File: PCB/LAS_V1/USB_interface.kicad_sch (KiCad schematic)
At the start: 3 parts, among them P1 USB_C_Plug

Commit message: installing JLB, PCB mostly done
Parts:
- removed D4: D_Schottky, symbol Device:D_Schottky
- removed P1: USB_C_Plug, symbol Connector:USB_C_Plug
- removed R5: 5.1k, symbol Device:R_Small_US
- added C10: 100uF, symbol Device:C_Small
- added C11, C7: 1uF/16V (10%), symbol Device:C_Small
- added C8, C9: 1uF, symbol Device:C_Small
- added D7: 1N5819WS, symbol Device:D_Schottky
- added J7: USB_C_Receptacle_USB2.0, symbol Connector:USB_C_Receptacle_USB2.0
- added Q2, Q3: MMBT2222A, symbol Simulation_SPICE:NPN
- added R10: 10k (1%), symbol Device:R_Small_US
- added R11, R12: 10k, symbol Device:R_Small_US
- added R8, R9: 5.1k, symbol Device:R_Small_US
- added U3: CH343P, Package_DFN_QFN:TQFN-16-1EP_3x3mm_P0.5mm_EP1.6x1.6mm, symbol Custom:CH343P
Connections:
- net GND: now also C10.2, C11.2, C7.2, C8.2, C9.2, J7.A1 (GND), J7.A12 (GND), J7.B1 (GND), J7.B12 (GND), R8.2, R9.2, U3.0 (GND), U3.17 (EP), U3.2 (GND)
- net VBus: now also C7.1, C9.1, D7.2 (A), J7.A4 (VBUS), J7.A9 (VBUS), J7.B4 (VBUS), J7.B9 (VBUS), U3.3 (VDD5), U3.4 (V3), U3.9 (VBUS)
- new net: Q2.2 (B), R12.2
- new net: C10.1, U3.6 (V3)
- new net: J7.A6 (D+), J7.B6 (D+), U3.7 (UD+)
- new net: J7.A7 (D-), J7.B7 (D-), U3.8 (UD-)
- new net: Q3.2 (B), R11.2
- new net: J7.B5 (CC2), R9.1
- new net: J7.A5 (CC1), R8.1
- new net +3.3V: C8.1, R10.1, U3.1 (VIO)
- new net BOOT_SEL: Q3.1 (C)
- new net CHIP_PU: C11.1, Q2.1 (C), R10.2
- new net DTR: Q3.3 (E), R12.1, U3.12 (DTR)
- new net RTS: Q2.3 (E), R11.1, U3.13 (RTS)
- new net RXD0: U3.4 (V3)
- new net TXD0: U3.5 (RXD)
- new net VCC_5V: D7.1 (K)
- no-connect marks 2 -> 8
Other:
- note added: "RTC_GPIO18, GPIO18, U1RXD, ADC2_CH7, DAC_2, CLK_OUT3"

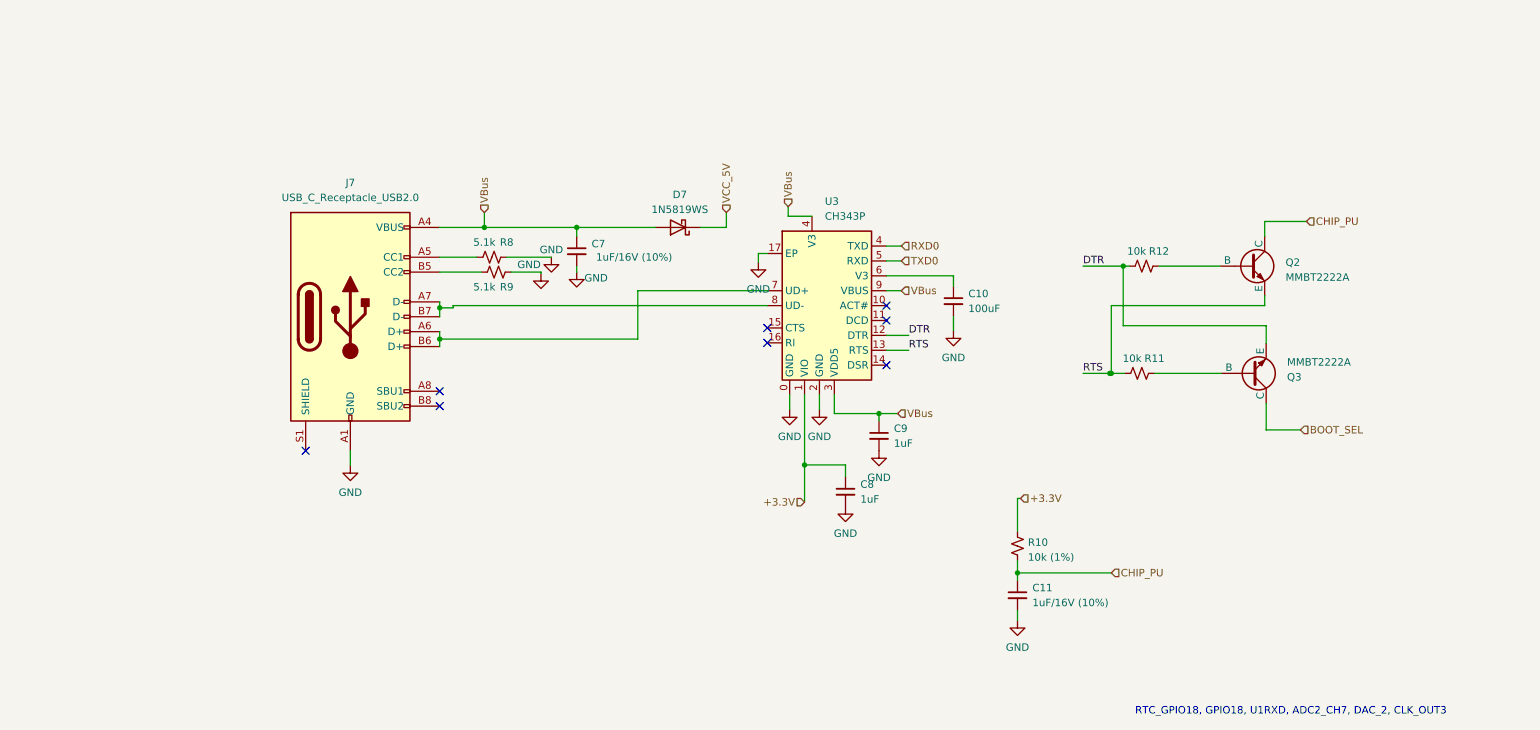
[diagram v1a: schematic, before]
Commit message: added JLBPCB part Numbers
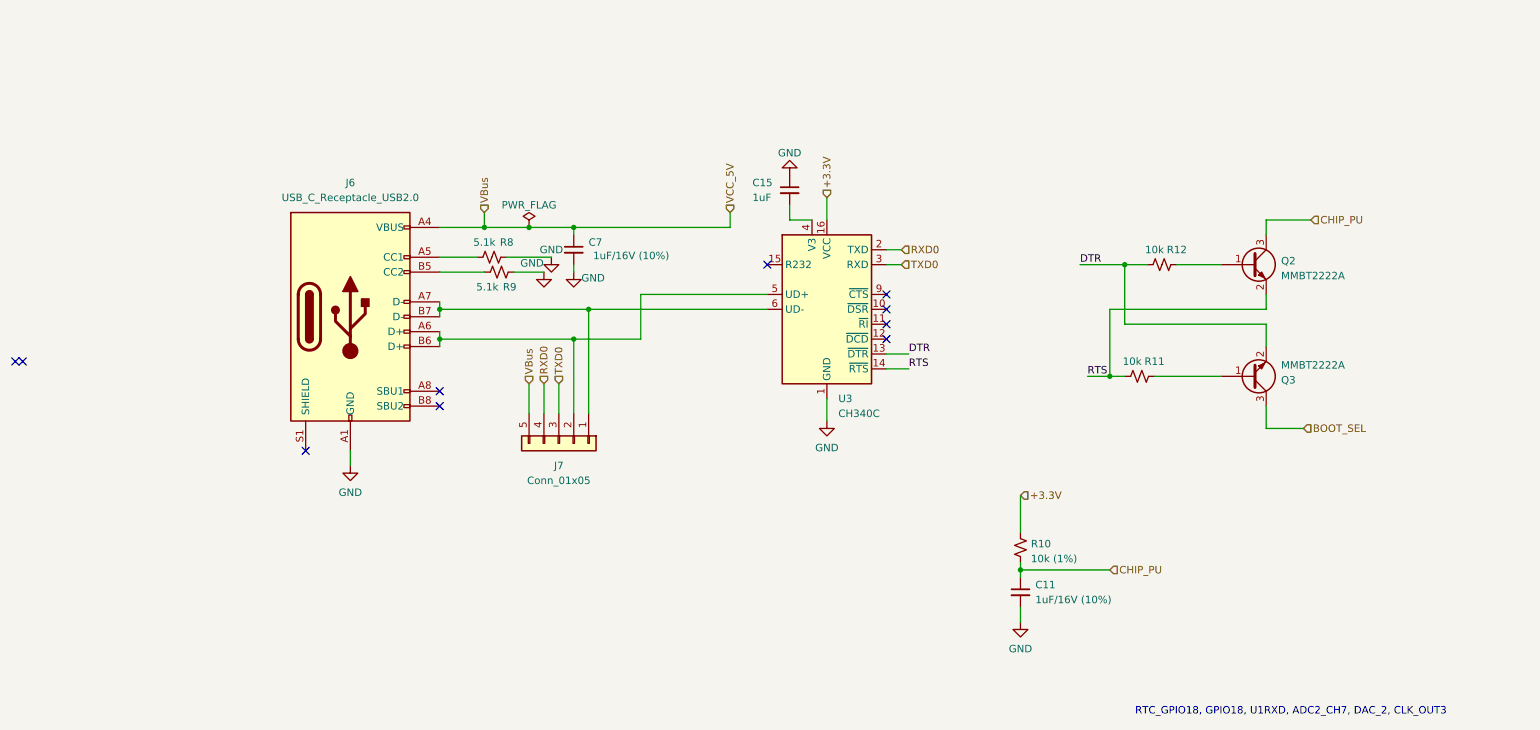
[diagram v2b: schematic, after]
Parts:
- removed C10: 100uF, symbol Device:C_Small
- removed C8, C9: 1uF, symbol Device:C_Small
- removed D7: 1N5819WS, symbol Device:D_Schottky
- removed Q2, Q3: MMBT2222A, symbol Simulation_SPICE:NPN
- removed U3: CH343P, Package_DFN_QFN:TQFN-16-1EP_3x3mm_P0.5mm_EP1.6x1.6mm, symbol Custom:CH343P
- added C15: 1uF, Capacitor_SMD:C_0603_1608Metric, symbol Device:C_Small
- added J7: Conn_01x05, Connector_PinHeader_1.27mm:PinHeader_1x05_P1.27mm_Vertical, symbol Connector_Generic:Conn_01x05
- added Q2, Q3: MMBT2222A, Package_TO_SOT_SMD:SOT-23, symbol Transistor_BJT:MMBT3904
- added U3: CH340C, Package_SO:SOIC-16_3.9x9.9mm_P1.27mm, symbol Interface_USB:CH340C
- C11, C7: footprint (none) -> Capacitor_SMD:C_0603_1608Metric; LCSC (none) -> C15849
- J6: renamed from J7; footprint (none) -> Custom:USB-C_SMD-TYPE-C-31-M-12; LCSC (none) -> C2927038
- R10: footprint (none) -> Resistor_SMD:R_0603_1608Metric; LCSC (none) -> C25804
- R11, R12: footprint (none) -> Resistor_SMD:R_1206_3216Metric; LCSC (none) -> C17902
- R8, R9: footprint (none) -> Resistor_SMD:R_0603_1608Metric; LCSC (none) -> C23186
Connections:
- net +3.3V: now also U3.16 (VCC)
- net BOOT_SEL: now also Q3.3 (C)
- net CHIP_PU: now also Q2.3 (C)
- net DTR: now also Q3.2 (E), U3.13 (~{DTR})
- net GND: now also C15.1, U3.1 (GND)
- net RTS: now also Q2.2 (E), U3.14 (~{RTS})
- net RXD0: now also J7.4 (Pin_4), U3.2 (TXD)
- net TXD0: now also J7.3 (Pin_3), U3.3 (RXD)
- net VBus: now also J7.5 (Pin_5)
- net at R12.2: now also Q2.1 (B)
- net at J6.A6 (D+), J6.B6 (D+): now also J7.2 (Pin_2), U3.5 (UD+)
- net at J6.A7 (D-), J6.B7 (D-): now also J7.1 (Pin_1), U3.6 (UD-)
- net at R11.2: now also Q3.1 (B)
- new net: C15.2, U3.4 (V3)
- no-connect marks 8 -> 10
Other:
- moved on the sheet: C11, C7, R10, R11, R12, R9

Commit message: All components Placed on PCB
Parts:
- renumbered C15 to C8, C11 to C9, J6 to J7, J7 to J8, R8 to R10, R9 to R11, R10 to R12, R11 to R13, R12 to R14
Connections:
- no-connect marks 10 -> 8
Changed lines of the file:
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@@
   (no_connect (at 101.6 83.82))
   (no_connect (at 157.48 59.69))
-  (no_connect (at 30.48 76.2))
   (no_connect (at 177.8 67.31))
   (no_connect (at 177.8 69.85))
   (no_connect (at 177.8 64.77))
-  (no_connect (at 29.21 76.2))
   (no_connect (at 177.8 72.39))
   (no_connect (at 78.74 91.44))
@@
     (stroke (width 0) (type default))
   )
-  (wire (pts (xy 177.8 77.47) (xy 181.61 77.47))
-    (stroke (width 0) (type default))
-  )
-  (wire (pts (xy 177.8 74.93) (xy 181.61 74.93))
+  (wire (pts (xy 177.8 77.47) (xy 187.96 77.47))
+    (stroke (width 0) (type default))
+  )
+  (wire (pts (xy 177.8 74.93) (xy 187.96 74.93))
     (stroke (width 0) (type default))
   )
@@
     (effects (font (size 1.27 1.27)) (justify left bottom))
   )
-  (label "RTS" (at 181.61 77.47 0) (fields_autoplaced)
+  (label "RTS" (at 187.96 77.47 0) (fields_autoplaced)
     (effects (font (size 1.27 1.27)) (justify left bottom))
   )
-  (label "DTR" (at 181.61 74.93 0) (fields_autoplaced)
+  (label "DTR" (at 187.96 74.93 0) (fields_autoplaced)
     (effects (font (size 1.27 1.27)) (justify left bottom))
   )
@@
   (symbol (lib_id "Device:R_Small_US") (at 224.79 59.69 90) (unit 1)
     (in_bom yes) (on_board yes) (dnp no)
-    (property "Reference" "R12" (at 227.33 57.15 90)
+    (property "Reference" "R14" (at 227.33 57.15 90)
       (effects (font (size 1.27 1.27)))
     )
@@
       (project "LAS_V1"
         (path "/aadef4b8-3115-4a49-998f-828f2021a6b4/a475df9f-c6e9-4f77-bf99-c031d1147f10"
-          (reference "R12") (unit 1)
+          (reference "R14") (unit 1)
         )
       )
@@
   (symbol (lib_id "Connector_Generic:Conn_01x05") (at 121.92 90.17 270) (unit 1)
     (in_bom yes) (on_board yes) (dnp no) (fields_autoplaced)
-    (property "Reference" "J7" (at 121.92 93.98 90)
+    (property "Reference" "J8" (at 121.92 93.98 90)
       (effects (font (size 1.27 1.27)))
     )
@@
       (project "LAS_V1"
         (path "/aadef4b8-3115-4a49-998f-828f2021a6b4/a475df9f-c6e9-4f77-bf99-c031d1147f10"
-          (reference "J7") (unit 1)
+          (reference "J8") (unit 1)
         )
       )
@@
   (symbol (lib_id "Device:C_Small") (at 200.66 115.57 0) (unit 1)
     (in_bom yes) (on_board yes) (dnp no) (fields_autoplaced)
-    (property "Reference" "C11" (at 203.2 114.3063 0)
+    (property "Reference" "C9" (at 203.2 114.3063 0)
       (effects (font (size 1.27 1.27)) (justify left))
     )
@@
       (project "LAS_V1"
         (path "/aadef4b8-3115-4a49-998f-828f2021a6b4/a475df9f-c6e9-4f77-bf99-c031d1147f10"
-          (reference "C11") (unit 1)
+          (reference "C9") (unit 1)
         )
       )
@@
   (symbol (lib_id "power:GND") (at 124.46 60.96 0) (unit 1)
     (in_bom yes) (on_board yes) (dnp no)
-    (property "Reference" "#PWR021" (at 124.46 67.31 0)
+    (property "Reference" "#PWR022" (at 124.46 67.31 0)
       (effects (font (size 1.27 1.27)) hide)
     )
@@
       (project "LAS_V1"
         (path "/aadef4b8-3115-4a49-998f-828f2021a6b4/a475df9f-c6e9-4f77-bf99-c031d1147f10"
-          (reference "#PWR021") (unit 1)
+          (reference "#PWR022") (unit 1)
         )
       )
@@
   (symbol (lib_id "power:GND") (at 120.65 58.42 0) (unit 1)
     (in_bom yes) (on_board yes) (dnp no)
-    (property "Reference" "#PWR020" (at 120.65 64.77 0)
+    (property "Reference" "#PWR021" (at 120.65 64.77 0)
       (effects (font (size 1.27 1.27)) hide)
     )
@@
       (project "LAS_V1"
         (path "/aadef4b8-3115-4a49-998f-828f2021a6b4/a475df9f-c6e9-4f77-bf99-c031d1147f10"
-          (reference "#PWR020") (unit 1)
+          (reference "#PWR021") (unit 1)
         )
       )
@@
   (symbol (lib_id "power:GND") (at 167.64 86.36 0) (unit 1)
     (in_bom yes) (on_board yes) (dnp no) (fields_autoplaced)
-    (property "Reference" "#PWR040" (at 167.64 92.71 0)
+    (property "Reference" "#PWR024" (at 167.64 92.71 0)
       (effects (font (size 1.27 1.27)) hide)
     )
@@
       (project "LAS_V1"
         (path "/aadef4b8-3115-4a49-998f-828f2021a6b4/a475df9f-c6e9-4f77-bf99-c031d1147f10"
-          (reference "#PWR040") (unit 1)
+          (reference "#PWR024") (unit 1)
         )
       )
@@
   (symbol (lib_id "Device:R_Small_US") (at 200.66 107.95 0) (unit 1)
     (in_bom yes) (on_board yes) (dnp no) (fields_autoplaced)
-    (property "Reference" "R10" (at 202.438 107.315 0)
+    (property "Reference" "R12" (at 202.438 107.315 0)
       (effects (font (size 1.27 1.27)) (justify left))
     )
@@
       (project "LAS_V1"
         (path "/aadef4b8-3115-4a49-998f-828f2021a6b4/a475df9f-c6e9-4f77-bf99-c031d1147f10"
-          (reference "R10") (unit 1)
+          (reference "R12") (unit 1)
         )
       )
@@
   (symbol (lib_id "Device:C_Small") (at 161.29 46.99 0) (unit 1)
     (in_bom yes) (on_board yes) (dnp no)
-    (property "Reference" "C15" (at 154.94 45.72 0)
+    (property "Reference" "C8" (at 154.94 45.72 0)
       (effects (font (size 1.27 1.27)) (justify left))
     )
@@
       (project "LAS_V1"
         (path "/aadef4b8-3115-4a49-998f-828f2021a6b4/a475df9f-c6e9-4f77-bf99-c031d1147f10"
-          (reference "C15") (unit 1)
+          (reference "C8") (unit 1)
         )
       )
@@
   (symbol (lib_id "Device:R_Small_US") (at 111.76 60.96 90) (unit 1)
     (in_bom yes) (on_board yes) (dnp no)
-    (property "Reference" "R9" (at 113.538 63.5 90)
+    (property "Reference" "R11" (at 113.538 63.5 90)
       (effects (font (size 1.27 1.27)))
     )
@@
       (project "LAS_V1"
         (path "/aadef4b8-3115-4a49-998f-828f2021a6b4/a475df9f-c6e9-4f77-bf99-c031d1147f10"
-          (reference "R9") (unit 1)
+          (reference "R11") (unit 1)
         )
       )
@@
   (symbol (lib_id "power:PWR_FLAG") (at 116.84 53.34 0) (unit 1)
     (in_bom yes) (on_board yes) (dnp no) (fields_autoplaced)
-    (property "Reference" "#FLG03" (at 116.84 51.435 0)
+    (property "Reference" "#FLG02" (at 116.84 51.435 0)
       (effects (font (size 1.27 1.27)) hide)
     )
@@
       (project "LAS_V1"
         (path "/aadef4b8-3115-4a49-998f-828f2021a6b4/a475df9f-c6e9-4f77-bf99-c031d1147f10"
-          (reference "#FLG03") (unit 1)
+          (reference "#FLG02") (unit 1)
         )
       )
@@
   (symbol (lib_id "power:GND") (at 119.38 60.96 0) (unit 1)
     (in_bom yes) (on_board yes) (dnp no)
-    (property "Reference" "#PWR019" (at 119.38 67.31 0)
+    (property "Reference" "#PWR020" (at 119.38 67.31 0)
       (effects (font (size 1.27 1.27)) hide)
     )
@@
       (project "LAS_V1"
         (path "/aadef4b8-3115-4a49-998f-828f2021a6b4/a475df9f-c6e9-4f77-bf99-c031d1147f10"
-          (reference "#PWR019") (unit 1)
+          (reference "#PWR020") (unit 1)
         )
       )
@@
   (symbol (lib_id "Device:R_Small_US") (at 110.49 58.42 90) (unit 1)
     (in_bom yes) (on_board yes) (dnp no)
-    (property "Reference" "R8" (at 113.03 55.88 90)
+    (property "Reference" "R10" (at 113.03 55.88 90)
       (effects (font (size 1.27 1.27)))
     )
@@
       (project "LAS_V1"
         (path "/aadef4b8-3115-4a49-998f-828f2021a6b4/a475df9f-c6e9-4f77-bf99-c031d1147f10"
-          (reference "R8") (unit 1)
+          (reference "R10") (unit 1)
         )
       )
@@
   (symbol (lib_id "power:GND") (at 86.36 93.98 0) (unit 1)
     (in_bom yes) (on_board yes) (dnp no) (fields_autoplaced)
-    (property "Reference" "#PWR018" (at 86.36 100.33 0)
+    (property "Reference" "#PWR019" (at 86.36 100.33 0)
       (effects (font (size 1.27 1.27)) hide)
     )
@@
       (project "LAS_V1"
         (path "/aadef4b8-3115-4a49-998f-828f2021a6b4/a475df9f-c6e9-4f77-bf99-c031d1147f10"
-          (reference "#PWR018") (unit 1)
+          (reference "#PWR019") (unit 1)
         )
       )
@@
   (symbol (lib_id "Connector:USB_C_Receptacle_USB2.0") (at 86.36 68.58 0) (unit 1)
     (in_bom yes) (on_board yes) (dnp no) (fields_autoplaced)
-    (property "Reference" "J6" (at 86.36 45.72 0)
+    (property "Reference" "J7" (at 86.36 45.72 0)
       (effects (font (size 1.27 1.27)))
     )
@@
       (project "LAS_V1"
         (path "/aadef4b8-3115-4a49-998f-828f2021a6b4/a475df9f-c6e9-4f77-bf99-c031d1147f10"
-          (reference "J6") (unit 1)
+          (reference "J7") (unit 1)
         )
       )
@@
   (symbol (lib_id "power:GND") (at 161.29 44.45 180) (unit 1)
     (in_bom yes) (on_board yes) (dnp no) (fields_autoplaced)
-    (property "Reference" "#PWR022" (at 161.29 38.1 0)
+    (property "Reference" "#PWR023" (at 161.29 38.1 0)
       (effects (font (size 1.27 1.27)) hide)
     )
@@
       (project "LAS_V1"
         (path "/aadef4b8-3115-4a49-998f-828f2021a6b4/a475df9f-c6e9-4f77-bf99-c031d1147f10"
-          (reference "#PWR022") (unit 1)
+          (reference "#PWR023") (unit 1)
         )
       )
@@
   (symbol (lib_id "power:GND") (at 200.66 120.65 0) (unit 1)
     (in_bom yes) (on_board yes) (dnp no) (fields_autoplaced)
-    (property "Reference" "#PWR028" (at 200.66 127 0)
+    (property "Reference" "#PWR025" (at 200.66 127 0)
       (effects (font (size 1.27 1.27)) hide)
     )
@@
       (project "LAS_V1"
         (path "/aadef4b8-3115-4a49-998f-828f2021a6b4/a475df9f-c6e9-4f77-bf99-c031d1147f10"
-          (reference "#PWR028") (unit 1)
+          (reference "#PWR025") (unit 1)
         )
       )
@@
   (symbol (lib_id "Device:R_Small_US") (at 220.98 78.74 90) (unit 1)
     (in_bom yes) (on_board yes) (dnp no)
-    (property "Reference" "R11" (at 223.52 76.2 90)
+    (property "Reference" "R13" (at 223.52 76.2 90)
       (effects (font (size 1.27 1.27)))
     )
@@
       (project "LAS_V1"
         (path "/aadef4b8-3115-4a49-998f-828f2021a6b4/a475df9f-c6e9-4f77-bf99-c031d1147f10"
-          (reference "R11") (unit 1)
-        )
-      )
+          (reference "R13") (unit 1)
+        )
+      )
